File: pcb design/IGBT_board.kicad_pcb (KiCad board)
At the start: 4 copper layers, 150 x 100 mm, 237 parts, among them J1 4-794627-0, J2 DESAT, J3 DESAT, Q1 IGBT, Q10 IGBT, Q11 IGBT, Q12 IGBT, Q13 NPN, Q14 PNP, Q15 CSD19533Q5A, Q16 CSD19533Q5A, Q17 NPN, Q18 PNP, Q19 PNP, Q2 IGBT, Q20 PNP, Q3 IGBT, Q4 IGBT, Q5 IGBT, Q6 IGBT, Q7 IGBT, Q8 IGBT, Q9 IGBT, T1 TRANS-3-1CT, U1 ISO5852S, U11 TLP2745, U12 OPA2172, U2 LM5030, U3 ISO5852S, U4 NAND, U5 APE8865U5-33-HF-3, U6 NAND, U7 NAND, U8 TLP2745, U9 OPA2172

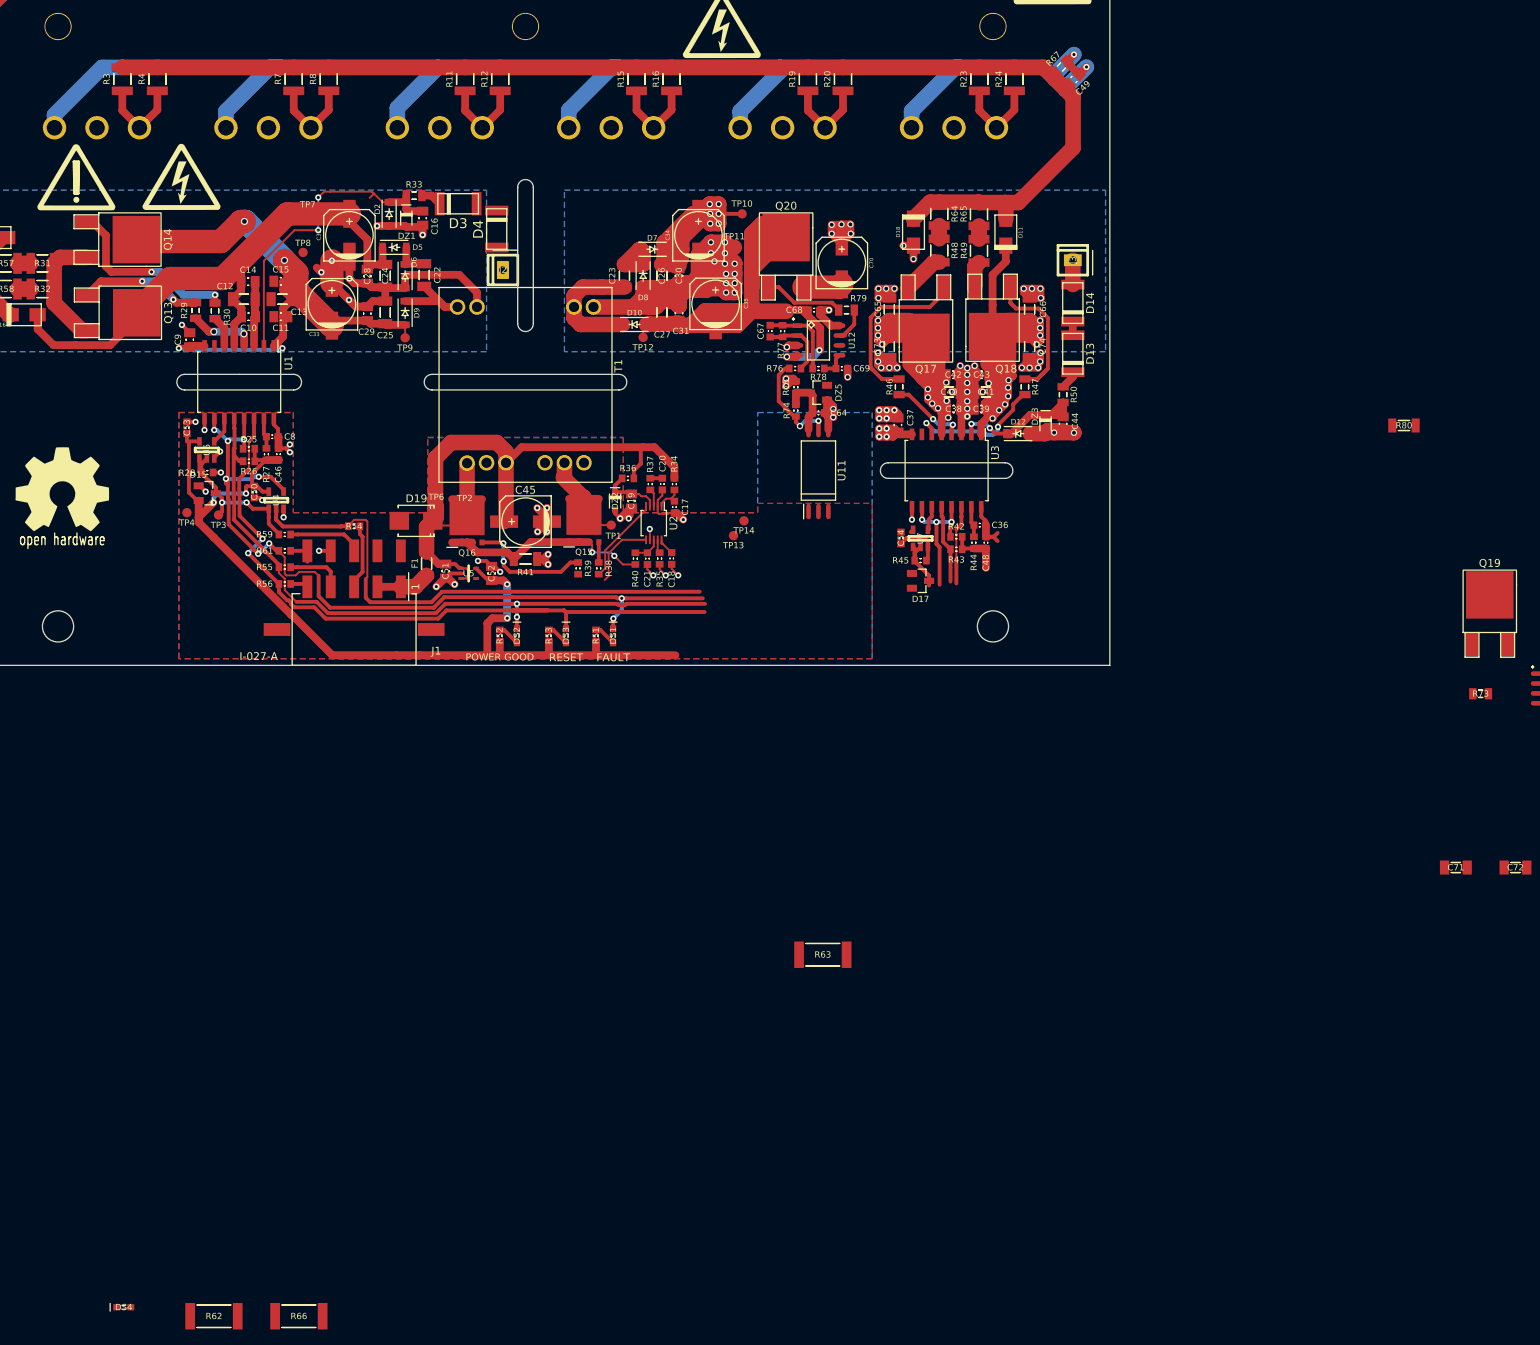
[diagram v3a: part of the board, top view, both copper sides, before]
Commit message: Updated copper planes. Added vias
Signed-off-by: Marcos Chaparro <mchaparro@paltatech.com>
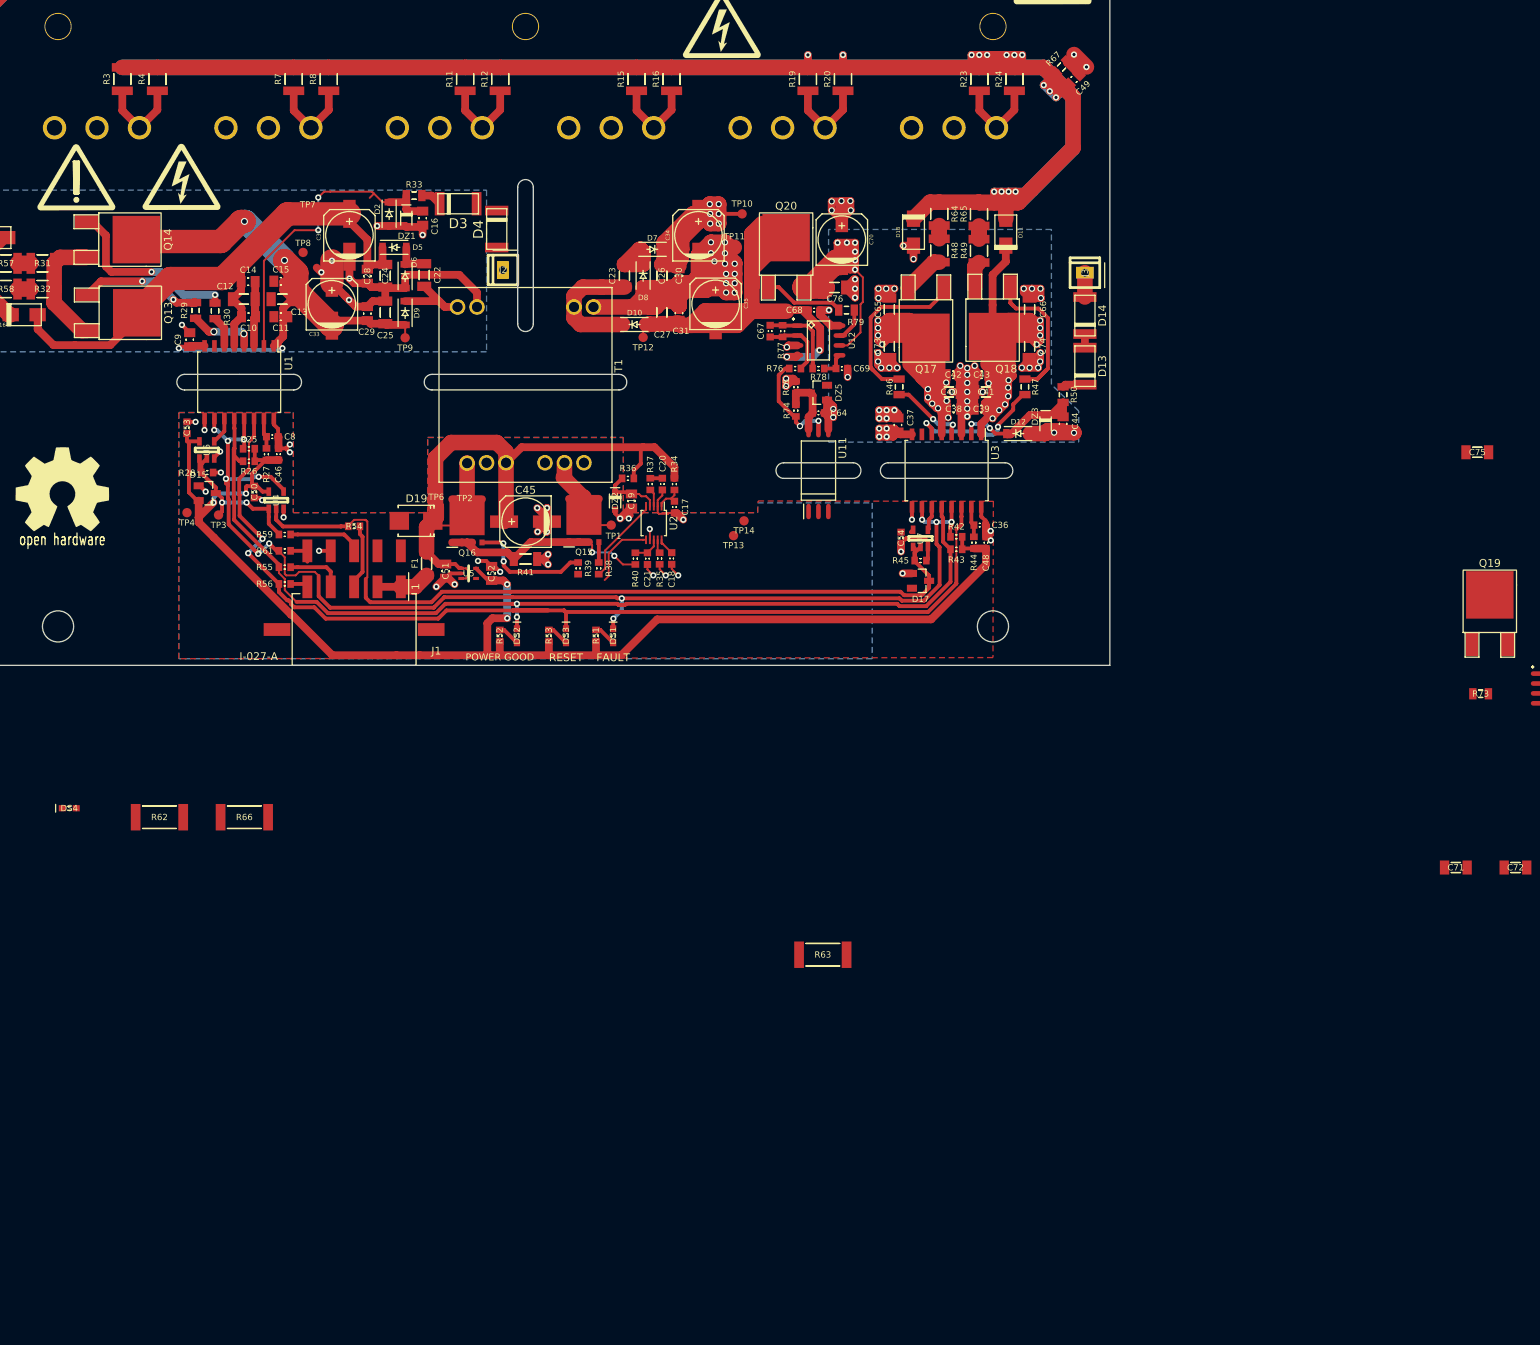
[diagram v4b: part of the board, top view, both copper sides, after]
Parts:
- removed R80: NI, IPC7351-Nominal:RESC3216X60
- added C75: 10uF 50v, IPC7351-Nominal:CAPC3216X70, F.Cu at (122.2, 22.7)
- added C76: 10uF 50v, IPC7351-Nominal:CAPC3216X70, F.Cu at (39.6, 1.50)
- moved DS4 64.4 mm to (-58.6, 68.3)
- moved R62 64.4 mm to (-47.0, 69.5)
- moved R66 64.4 mm to (-36.1, 69.5)
- moved C70 3.00 mm to (40.6, -4.65)
- moved J3 2.23 mm to (71.8, -0.40)
- moved D13 2.23 mm to (71.8, 11.6)
- moved D14 2.23 mm to (71.8, 5.10)
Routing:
- net VBUS-: track 372.1 -> 614.1 mm, vias 60 -> 63
- net GATE_LOW: track 156.5 -> 389.7 mm, vias 0 -> 15
- net 3.3v: track 133.6 -> 177.9 mm
- net /RESET: track 89.9 -> 133.9 mm
- net /PWR_GOOD: track 97.1 -> 130.1 mm
- net /FAULT: track 122.5 -> 153.9 mm
- net /IN_BOTTOM: track 75.4 -> 106.4 mm
- net /IGBT_driver_BOT/-VEE: track 82.2 -> 110.9 mm, vias 15 -> 21
- net /IGBT_driver_TOP/-8V: track 28.5 -> 46.6 mm, vias 0 -> 2
- net /IGBT_driver_TOP/-VEE: track 64.5 -> 46.5 mm, vias 4 -> 2
- net (no net): track 11.8 -> 0.00 mm, vias 1 -> 0
- net GND: track 69.0 -> 72.1 mm, vias 27 -> 32
- net Net-(D13-Pad2): track 2.39 -> 2.91 mm
- added copper zone on PWR.Cu, net /IGBT_driver_BOT/+15V
- added copper zone on B.Cu, net /IGBT_driver_BOT/-VEE
- added copper zone on GNDs.Cu, net VBUS-
- removed copper zone on GNDs.Cu, net PHASE
- removed copper zone on PWR.Cu, net VBUS+
- removed copper zone on B.Cu, net VBUS-
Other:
- outline, holes or cut-outs redrawn

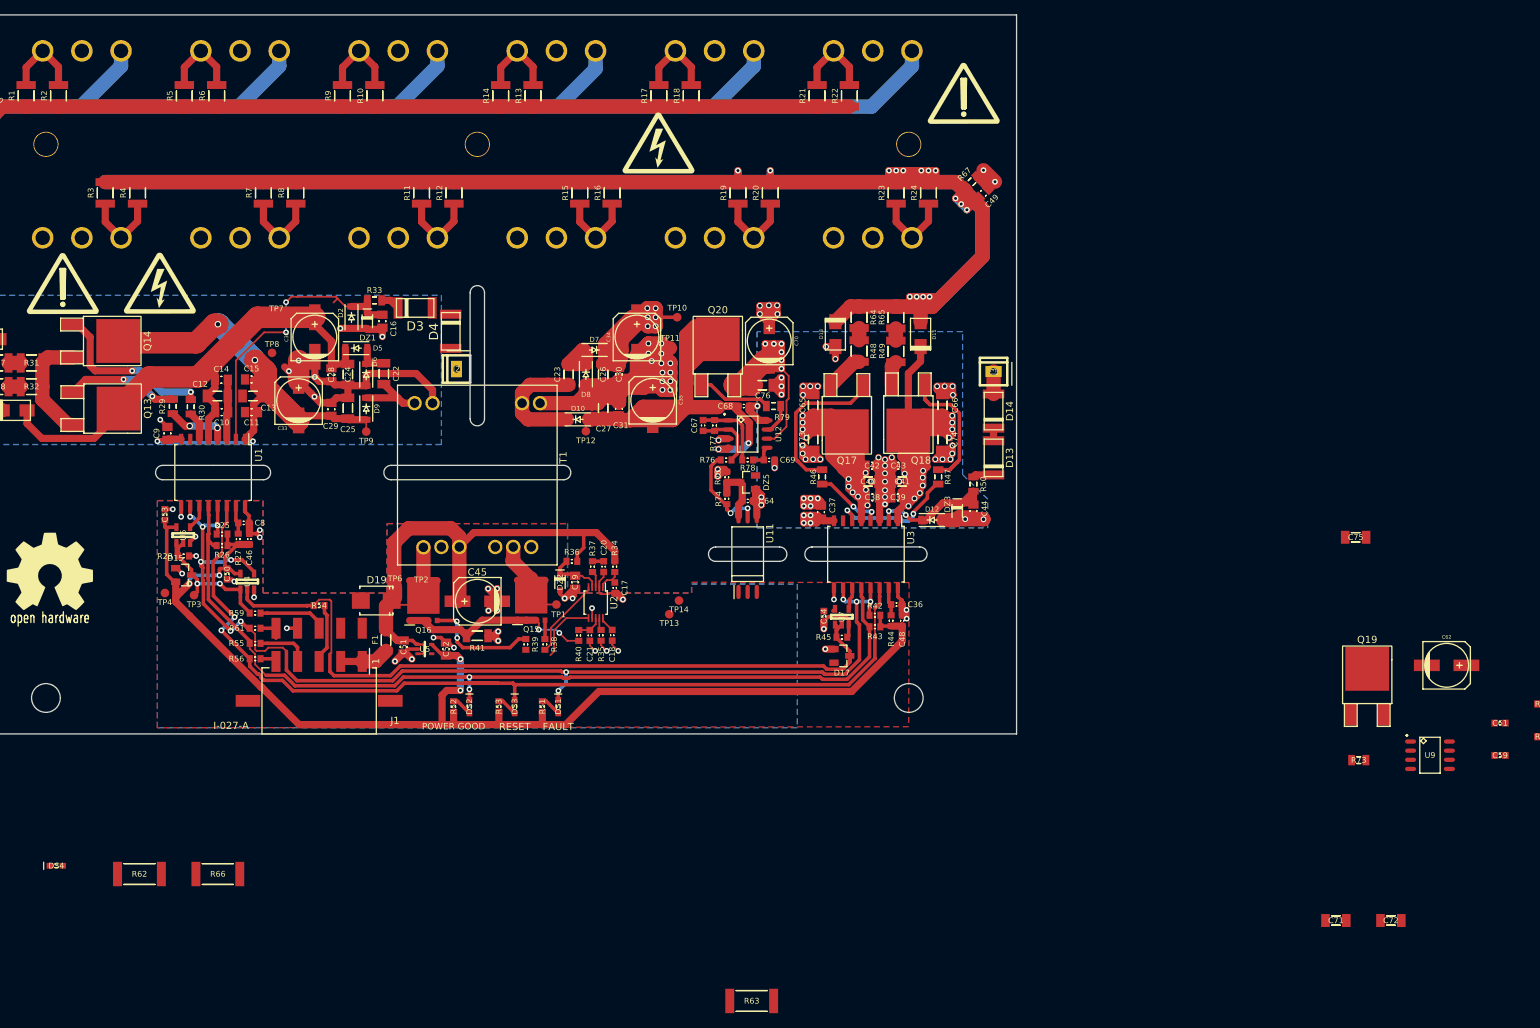
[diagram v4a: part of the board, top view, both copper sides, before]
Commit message: Improved gate traces using 4 layers. Increased TO-247 creepage with slots
Signed-off-by: Marcos Chaparro <mchaparro@paltatech.com>
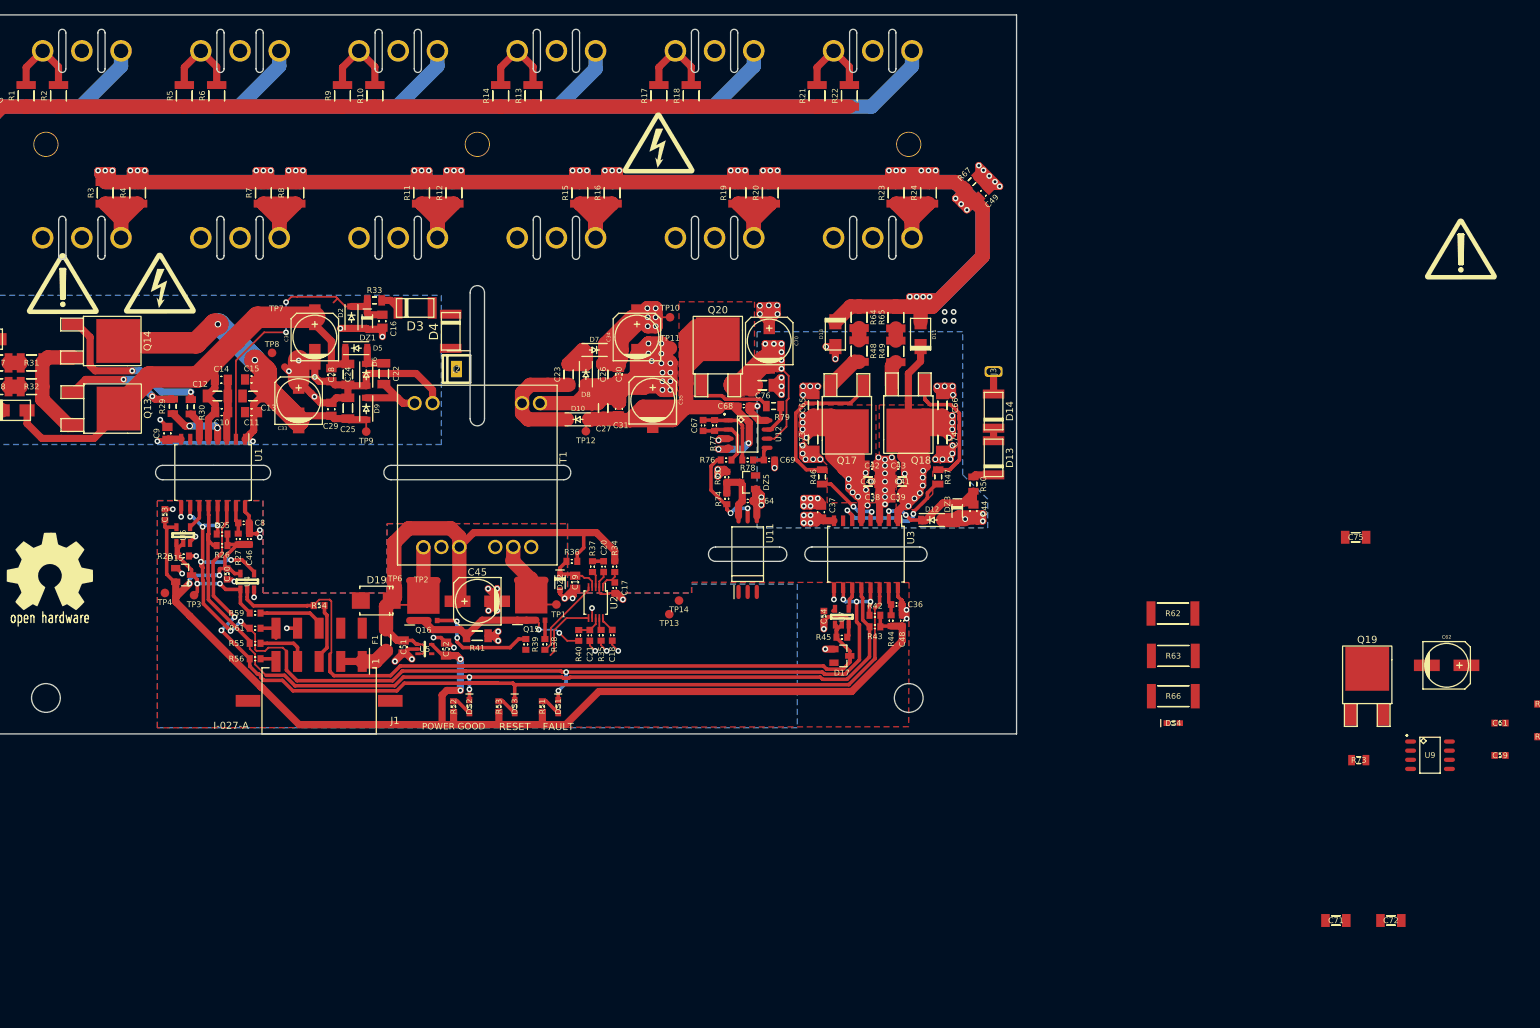
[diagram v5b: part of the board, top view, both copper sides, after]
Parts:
- Q1, Q10, Q11, Q12, Q2, Q3, Q4, Q5, Q6, Q7, Q8, Q9: footprint pth-semi:TO-247 -> pth-semi:TO-247-HV
- moved DS4 156.6 mm to (96.8, 48.5)
- moved R62 148.2 mm to (96.8, 33.2), turned to 180 degrees
- moved R66 135.2 mm to (96.8, 44.8), turned to 180 degrees
- moved R63 75.8 mm to (96.8, 39.1)
- moved G*** 72.5 mm to (136.8, -17.4)
- moved TP10 1.00 mm to (26.8, -7.95)
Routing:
- net GATE_LOW: track 389.7 -> 533.4 mm, vias 15 -> 43
- net VBUS-: track 614.1 -> 667.0 mm, vias 63 -> 71
- net Net-(Q12-Pad1): track 11.4 -> 20.6 mm
- net Net-(Q8-Pad1): track 11.4 -> 15.9 mm
- net Net-(Q6-Pad1): track 11.4 -> 15.9 mm
- net Net-(Q4-Pad1): track 11.4 -> 15.9 mm
- net Net-(Q2-Pad1): track 11.4 -> 15.9 mm
- net Net-(Q10-Pad1): track 11.4 -> 15.9 mm
- net /IGBT_driver_BOT/+15V: track 108.8 -> 107.8 mm
- added copper zone on F.Cu, net /IGBT_driver_BOT/+15V
- added copper zone on F.Cu, net /IGBT_driver_BOT/-8V
- added copper zone on F.Cu, net /IGBT_driver_BOT/-VEE
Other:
- rule pad_to_mask_clearance: 0.2 -> 0.15
